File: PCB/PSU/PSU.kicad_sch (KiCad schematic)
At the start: 258 parts, among them J1 Backllight_Connector, J2 PSU_Jack, J3 PSU_Connector_Receptor, Q1 R4C, Q10 103 5G, Q11 6LS, Q12 Q, Q13 8LR, Q14 6LS, Q15 8LR, Q16 M2P, Q17 M2P, Q18 Q, Q19 M2P, Q2 K, Q20 W6, Q21 8C, Q22 8C, Q23 8C, Q24 6LS, Q25 8LB, Q26 G16, Q27 8C, Q28 W6, Q29 H15, Q3 6LS, Q30 8C, Q31 W6, Q32 K, Q33 8LR, Q34 6LS, Q35 8C, Q36 3P4J, Q37 8LR, Q4 8LR, Q5 8C, Q6 6LS, Q7 6LS, Q8 303 5H, Q9 KD 3.E, SW1 PSU-SW1, U1 D9D, U10 9742, U11 7W14, U12 J421, U13 J421, U2 TA, U3 6.5 5F, U4 MAX786CAI, U5 K2337, U6 7064, U7 5W01, U8 2556, U9 2556

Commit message: cleanup psu schematics
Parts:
- removed C1, C16, C24, C28, C36, C46, C47, C5, C59, C7: 150nF, Capacitor_SMD:C_0603_1608Metric, symbol PCM_Elektuur:C
- removed C10: 3.6nF, Capacitor_SMD:C_0603_1608Metric, symbol PCM_Elektuur:C
- removed C11, C15, C37, C44, C49: 180nF, Capacitor_SMD:C_0603_1608Metric, symbol PCM_Elektuur:C
- removed C12: 1.2uF, Capacitor_SMD:C_1206_3216Metric, symbol PCM_Elektuur:C
- removed C13, C14: 1.5uF, Capacitor_SMD:C_1206_3216Metric, symbol PCM_Elektuur:C
- removed C17, C22, C26, C29, C30, C32, C39, C40, C48, C9: 10nF, Capacitor_SMD:C_0603_1608Metric, symbol PCM_Elektuur:C
- removed C18, C42, C51, C53, C64: 120nF, Capacitor_SMD:C_0603_1608Metric, symbol PCM_Elektuur:C
- removed C19: 18nF, Capacitor_SMD:C_0603_1608Metric, symbol PCM_Elektuur:C
- removed C2: 4.7nF, Capacitor_SMD:C_0603_1608Metric, symbol PCM_Elektuur:C
- removed C20, C6: 100pF, Capacitor_SMD:C_0603_1608Metric, symbol PCM_Elektuur:C
- removed C21: 12nF, Capacitor_SMD:C_0603_1608Metric, symbol PCM_Elektuur:C
- removed C23, C34, C38, C41, C55, C58: 1.5uF, Capacitor_SMD:C_0805_2012Metric, symbol PCM_Elektuur:C
- removed C25, C27, C31, C35, C66: 1.2nF, Capacitor_SMD:C_0603_1608Metric, symbol PCM_Elektuur:C
- removed C3: 5.2uF, Capacitor_SMD:C_1206_3216Metric, symbol PCM_Elektuur:C
- removed C33, C8: 24nF, Capacitor_SMD:C_0603_1608Metric, symbol PCM_Elektuur:C
- removed C4: 2.5nF, Capacitor_SMD:C_0603_1608Metric, symbol PCM_Elektuur:C
- removed C43: 10pF, Capacitor_SMD:C_0603_1608Metric, symbol PCM_Elektuur:C
- removed C45: 33uF 20V, Capacitor_THT:C_Disc_D3.0mm_W1.6mm_P2.50mm, symbol PCM_Elektuur:C
- removed C50: 56uF 25V EC, Capacitor_THT:EC, symbol PCM_Elektuur:C
- removed C52, C60: 1nF, Capacitor_SMD:C_0603_1608Metric, symbol PCM_Elektuur:C
- removed C54, C61: 47uF 6.3v, Capacitor_THT:C_Radial_D6.3mm_H11.0mm_P2.50mm, symbol PCM_Elektuur:C
- removed C56: 47uF 6.3V, Capacitor_THT:C_Radial_D6.3mm_H11.0mm_P2.50mm, symbol PCM_Elektuur:C
- removed C57: 15uF 16V, Capacitor_THT:C_Radial_D6.3mm_H11.0mm_P2.50mm, symbol PCM_Elektuur:C
- removed C62, C65: 100nF, Capacitor_SMD:C_0603_1608Metric, symbol PCM_Elektuur:C
- removed C63: 5.1nF, Capacitor_SMD:C_0603_1608Metric, symbol PCM_Elektuur:C
- removed C67: 18uF 50V, Capacitor_THT:C_Radial_D6.3mm_H11.0mm_P2.50mm, symbol PCM_Elektuur:C
- removed D1: 8-2, Diode_SMD:D_0603_1608Metric, symbol Device:D_Zener
- removed D2: 5-9, Diode_SMD:D_0603_1608Metric, symbol PCM_Elektuur:D
- removed D3: DNP, Diode_SMD:D_1206_3216Metric, symbol PCM_Elektuur:C
- removed D4: 18, Diode_SMD:D_0603_1608Metric, symbol Device:D
- removed D5: 3^9, Diode_SMD:D_0603_1608Metric, symbol Device:D
- removed D6: DNP, Diode_SMD:D_1206_3216Metric, symbol PCM_Elektuur:R
- removed D7, D8: s.3 4F, Diode_SMD:D_1206_3216Metric, symbol PCM_Elektuur:D
- removed F1, F5: 2.5A, Fuse:Fuse_2010_5025Metric, symbol Device:Fuse
- removed F2: 830mA, Fuse:Fuse_2010_5025Metric, symbol Device:Fuse
- removed F3: 15, Fuse:Fuse_1206_3216Metric, symbol Device:Fuse
- removed F4: 10, Fuse:Fuse_1210_3225Metric, symbol Device:Fuse
- removed J1: Backllight_Connector, Connector_JST:Backllight_Connector, symbol Connector_Generic:Conn_01x04
- removed J2: PSU_Jack, PSU:PSU_Jack, symbol Connector:Jack-DC
- removed J3: PSU_Connector_Receptor, PSU:PSU_Connector_Receptor, symbol Connector_Generic:Conn_02x20_Top_Bottom
- removed JX1: Main Battery, symbol Connector:Conn_01x02_Pin
- removed L1: 10uH, Inductor_THT:L_Radial_D7.5mm_P5.00mm_Fastron_07P, symbol PCM_Elektuur:L
- removed L2, L5: 10uH, Inductor_THT:L_Radial_D10.0mm_P5.00mm_Fastron_07M, symbol PCM_Elektuur:L
- removed L3: 68uH, Inductor_SMD:L_Coilcraft_LPS5030, symbol PCM_Elektuur:L
- removed L4: 470uH, Inductor_SMD:L_Coilcraft_LPS5030, symbol PCM_Elektuur:L
- removed Q1: R4C, PC110:3D, symbol Device:D_Zener_Dual_CommonCathode_AAK_Split
- removed Q10: 103 5G, Package_TO_SOT_SMD:SOT-powerT, symbol PSU:103_5G
- removed Q11, Q14: 6LS, Package_TO_SOT_SMD:SOT-416, symbol PCM_Transistor_BJT_AKL:Q_PNP_Generic_BEC
- removed Q12: Q, PC110:3D, symbol Device:D_Zener_Dual_CommonAnode_KAK
- removed Q13, Q15, Q33, Q37: 8LR, Package_TO_SOT_SMD:SOT-416, symbol PCM_Transistor_BJT_AKL:Q_NPN_Generic_BEC
- removed Q16, Q17, Q19: M2P, PC110:3D, symbol Device:D_Zener_Dual_CommonAnode_KAK
- removed Q18: Q, PC110:3D, symbol Device:D_Dual_CommonCathode_AKA
- removed Q2: K, PC110:3D, symbol Device:D_Dual_Series_KAC_Parallel
- removed Q20, Q28, Q31: W6, PC110:3D, symbol Device:D_Dual_CommonCathode_AKA
- removed Q21: 8C, Package_TO_SOT_SMD:SOT-416, symbol Simulation_SPICE:NPN
- removed Q22, Q5: 8C, Package_TO_SOT_SMD:SOT-416, symbol PCM_Transistor_BJT_AKL:Q_NPN_Generic_CEB
- removed Q23, Q27, Q30, Q35: 8C, Package_TO_SOT_SMD:SOT-416, symbol PCM_Transistor_BJT_AKL:Q_NPN_Generic_BEC
- removed Q24: 6LS, Package_TO_SOT_SMD:SOT-416, symbol PCM_Transistor_BJT_AKL:Q_PNP_Generic_CEB
- removed Q25: 8LB, Package_TO_SOT_SMD:SOT-416, symbol PCM_Transistor_BJT_AKL:Q_NPN_Generic_BEC
- removed Q26: G16, Package_TO_SOT_SMD:SOT-23-PC110, symbol PCM_Transistor_MOSFET_AKL:2N7002AQ
- removed Q29: H15, Package_TO_SOT_SMD:SOT-23-PC110, symbol Transistor_FET:AO3401A
- removed Q3, Q34, Q6, Q7: 6LS, Package_TO_SOT_SMD:SOT-416, symbol Simulation_SPICE:PNP
- removed Q32: K, PC110:3D, symbol Device:D_Dual_Series_ACK_Parallel
- removed Q36: 3P4J, Package_TO_SOT_SMD:TO-252-2, symbol PCM_Elektuur:Th
- removed Q4: 8LR, Package_TO_SOT_SMD:SOT-416, symbol PCM_Transistor_BJT_AKL:Q_NPN_Generic_CEB
- removed Q8: 303 5H, Package_TO_SOT_SMD:SOT-powerT, symbol PSU:103_5G
- removed Q9: KD 3.E, Package_TO_SOT_SMD:SOT-89-3, symbol Regulator_Linear:L78L05_SOT89
- removed R1, R108, R50, R82: DNP, Resistor_SMD:R_0603_1608Metric, symbol PCM_Elektuur:R
- removed R10, R2, R21, R31, R70, R74, R83, R87, R90: 470k, Resistor_SMD:R_0603_1608Metric, symbol PCM_Elektuur:R
- removed R100, R110: 7.5k, Resistor_SMD:R_0603_1608Metric, symbol PCM_Elektuur:R
- removed R101, R109, R45, R62, R69, R81: 200k, Resistor_SMD:R_0603_1608Metric, symbol PCM_Elektuur:R
- removed R102, R49, R53, R78: 300k, Resistor_SMD:R_0603_1608Metric, symbol PCM_Elektuur:R
- removed R103, R11, R114, R117, R13, R17, R19, R20, R30, R33, R35, R4, R44, R52, R61, R63, R64, R85, R86: 10k, Resistor_SMD:R_0603_1608Metric, symbol PCM_Elektuur:R
- removed R104, R118, R48: 100, Resistor_SMD:R_0603_1608Metric, symbol PCM_Elektuur:R
- removed R105, R15, R22, R5, R54, R57, R59, R77, R80, R84, R92: 100k, Resistor_SMD:R_0603_1608Metric, symbol PCM_Elektuur:R
- removed R106, R27, R39, R41, R51, R58, R60: 4.7k, Resistor_SMD:R_0603_1608Metric, symbol PCM_Elektuur:R
- removed R107: 2k, Resistor_SMD:R_0603_1608Metric, symbol PCM_Elektuur:R
- removed R111: 33, Resistor_SMD:R_0603_1608Metric, symbol PCM_Elektuur:R
- removed R112, R113, R18, R9: 20k, Resistor_SMD:R_0603_1608Metric, symbol PCM_Elektuur:R
- removed R115: 11K, Resistor_SMD:R_0603_1608Metric, symbol PCM_Elektuur:R
- removed R116: 15k, Resistor_SMD:R_0603_1608Metric, symbol PCM_Elektuur:R
- removed R12: 2.2k, Resistor_SMD:R_0603_1608Metric, symbol PCM_Elektuur:R
- removed R14: 12k, Resistor_SMD:R_0603_1608Metric, symbol PCM_Elektuur:R
- removed R16: 130k, Resistor_SMD:R_0603_1608Metric, symbol PCM_Elektuur:R
- removed R23, R25, R32, R34: 0.1, Resistor_SMD:R_1206_3216Metric, symbol PCM_Elektuur:R
- removed R24: 220, Resistor_SMD:R_0603_1608Metric, symbol PCM_Elektuur:R
- removed R26: 103 (RT1), Resistor_SMD:R_1206_3216Metric, symbol PCM_Elektuur:R
- removed R28: 0, Resistor_SMD:R_0603_1608Metric, symbol PCM_Elektuur:R
- removed R29: 103 (RT2), Resistor_SMD:R_1206_3216Metric, symbol PCM_Elektuur:R
- removed R3, R36, R65, R71, R72, R75, R76, R93: 1k, Resistor_SMD:R_0603_1608Metric, symbol PCM_Elektuur:R
- removed R37: 120, Resistor_SMD:R_0603_1608Metric, symbol PCM_Elektuur:R
- removed R38, R6: 470, Resistor_SMD:R_0603_1608Metric, symbol PCM_Elektuur:R
- removed R40: 0.22, Resistor_SMD:R_1206_3216Metric, symbol PCM_Elektuur:R
- removed R42, R47, R67, R68, R73, R79, R94: 47k, Resistor_SMD:R_0603_1608Metric, symbol PCM_Elektuur:R
- removed R43, R56: 300, Resistor_SMD:R_0603_1608Metric, symbol PCM_Elektuur:R
- removed R46, R55, R88, R89: 1M, Resistor_SMD:R_0603_1608Metric, symbol PCM_Elektuur:R
- removed R66: DNP, Resistor_SMD:R_0603_1608Metric, symbol PCM_Elektuur:C
- removed R7, R8: 0.1, Resistor_SMD:R_1210_3225Metric, symbol PCM_Elektuur:R
- removed R91: DNP, Resistor_SMD:R_1206_3216Metric, symbol PCM_Elektuur:R
- removed R95, R97: DNP, Resistor_SMD:R_1206_3216Metric, symbol PCM_Elektuur:C
- removed R96: 1.8k, Resistor_SMD:R_0603_1608Metric, symbol PCM_Elektuur:R
- removed R98, R99: 0, Resistor_SMD:R_1206_3216Metric, symbol PCM_Elektuur:R
- removed SW1: PSU-SW1, PSU:PSU-SW1, symbol Switch:SW_Push
- removed U1: D9D, Package_TO_SOT_SMD:SOT-23-5, symbol Power_Management:BD48ExxG
- removed U10: 9742, Package_SO:SSOP-16_4.4x5.2mm_P0.65mm, symbol PSU:9742
- removed U11: 7W14, PSU:SSOP-8-PSU, symbol 74xGxx:74LVC3G14
- removed U12, U13: J421, Package_SO:SOP-8_3.9x4.9mm_P1.27mm, symbol Transistor_FET:FDS2734
- removed U2: TA, Package_TO_SOT_SMD:SOT-23-5, symbol PSU:TA
- removed U3: 6.5 5F, Package_TO_SOT_SMD:SOT-23-6_Handsoldering, symbol PSU:6.5_5F
- removed U4: MAX786CAI, Package_SO:TSSOP-28_6.1x9.7mm_P0.65mm, symbol PSU:MAX786CAI
- removed U5: K2337, Package_SO:SOP-8_3.9x4.9mm_P1.27mm, symbol Transistor_FET:Si4542DY
- removed U6: 7064, Package_SO:TSSOP-14_4.4x5mm_P0.65mm, symbol Device:Opamp_Quad
- removed U7: 5W01, PSU:SSOP-8-PSU, symbol Device:Opamp_Dual
- removed U8, U9: 2556, Package_SO:SOP-8_3.9x4.9mm_P1.27mm, symbol Transistor_FET:FDS2734
- added C65: 0.1u, symbol PSU:C
- added CN3: 179029-1, symbol PSU:CN_40
- added CN4: DF13- 4P-1.25V, symbol PSU:CN_4+PAD
- added D10: MA741WA, symbol PSU:D_ANODE-COM
- added D11: MAZ8039-H, symbol PSU:Z
- added F6: 630mA, symbol PSU:F
- added R107: 1k, symbol PSU:R
- added R108: 47k, symbol PSU:R
- added R109, R110: 4.7k, symbol PSU:R
- added R111: (no value), symbol PSU:R
- added RT1, RT2: 103HT-xx, symbol PSU:RL
- added SW1: (no value), symbol PSU:SW_PAD
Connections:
- net GND: now also C65.1, CN3.24, CN3.25, CN3.29, CN3.32, CN3.37, CN3.5, CN3.7, CN3.9, CN4.3, R108.2, R109.1, R110.1
- new net: D10.1 (C1), R110.2, RT2.2
- new net: D10.2 (A), D11.1 (C), R111.1
- new net: D10.3 (C2), R109.2, RT1.1
- new net: C65.2, CN4.4, F6.1
- new net: R107.1, R108.1, SW1.2
- new net +12V: CN3.12
- new net +12V_ENABLE: CN3.34
- new net +3V3: CN3.28, CN3.8
- new net +5V_STBY: CN3.16, SW1.1
- new net +5V_SW: CN3.10, CN3.11, CN3.31, RT1.2, RT2.1
- new net BAT_MONT_VOLT: CN3.21
- new net BAT_MON_CHGCURR: CN3.2
- new net BAT_MON_DISCHGCURR: CN3.1
- new net CHG_CONT_1: CN3.19
- new net CHG_CONT_2: CN3.39
- new net CHG_MONPWR_EN: CN3.18
- new net CHG_SUBPWR: CN3.6
- new net EXT_DEV_DETSW: CN3.33, R107.2
- new net LCD_BKLIT_ADJ: CN3.20, CN4.2
- new net LCD_BKLIT_INVEN: CN3.40, CN4.1
- new net MONT_VOLT_ENABLE: CN3.38
- new net TEMPSENS: CN3.22, D11.2 (A), R111.2
- new net VAA_LCD: CN3.13
- new net VAA_LCD_ADJ: CN3.15
- new net VAA_LCD_ENABLE: CN3.35
- new net VIN_AC_DETECT: CN3.26
- new net VIN_AC_MON_VOLT: CN3.27
- new net VREF: CN3.30
- new net VSW: CN3.14, F6.2
- new net VSW_ENABLE_1: CN3.17
- new net VSW_ENABLE_2: CN3.36
- new net VSYS: CN3.23, CN3.3, CN3.4
- no-connect marks 3 -> 2
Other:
- added sheet AC Input (acinput.kicad_sch)
- added sheet Battery Charge, Monitor (batchgmon.kicad_sch)
- added sheet DC-DC (dcdc.kicad_sch)
- added sheet Standby Power (stdbypwr.kicad_sch)
- note added: "+12V"
- note added: "+3.3"
- note added: "+5V"
- note added: "+5V_STBY"
- note added: "LCD_VAA"
- note added: "SOC SSFC? Quick-Acting"
- note added: "VSW"
- note added: "VSYS"
- company: Recreated by: Ahmad Byagowi -> (none)
- title: PC110 Power Supply Unit -> IBM 39H4552 : PalmTop PC110 Power supply module

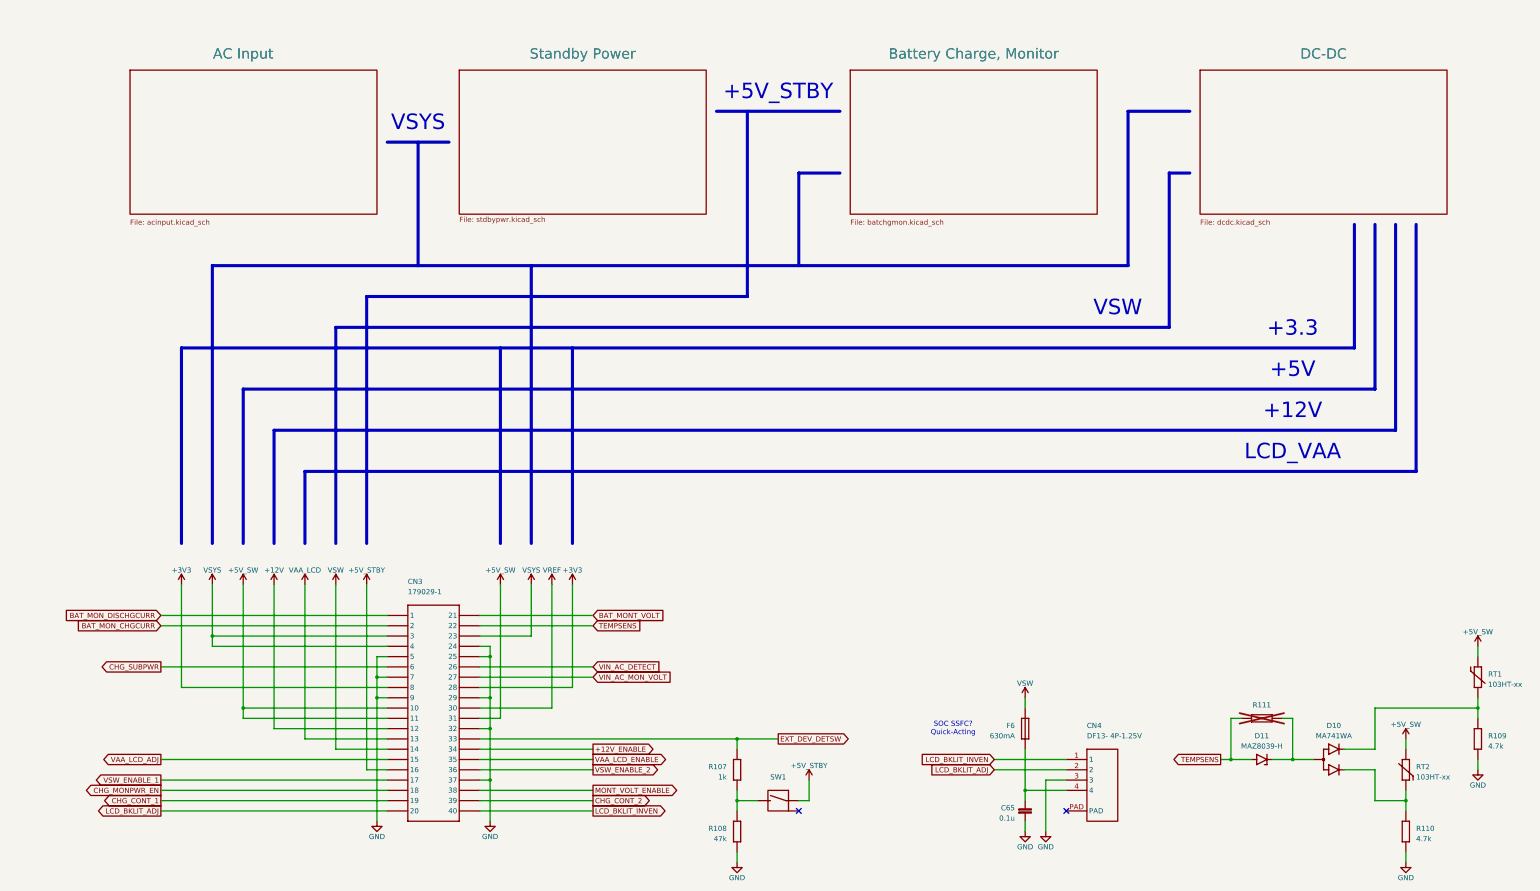
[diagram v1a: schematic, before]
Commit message: edit layout and misspelled word(not changed sch)
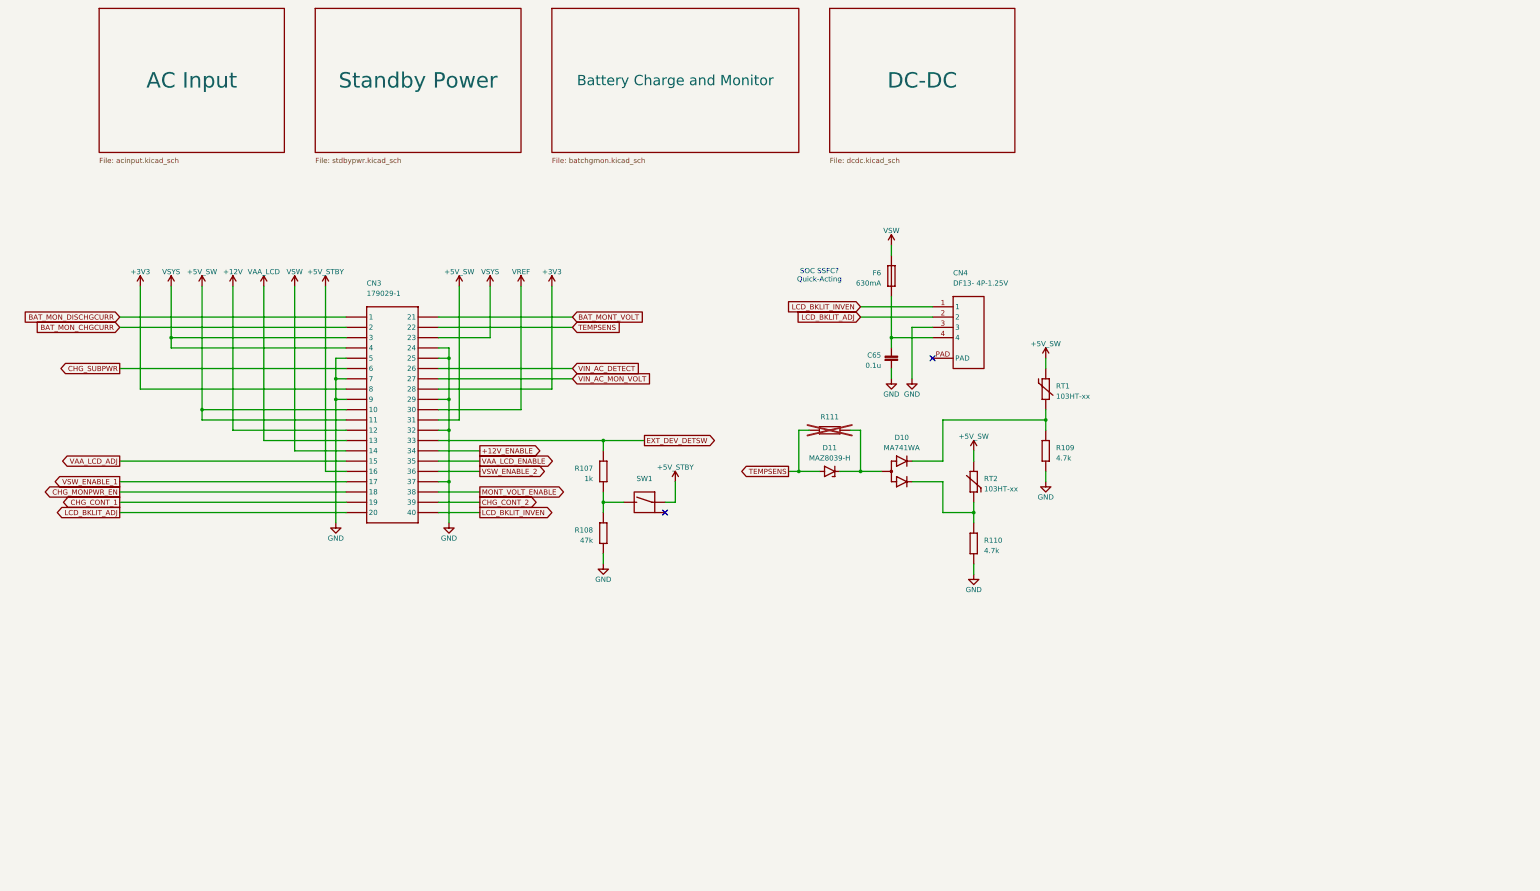
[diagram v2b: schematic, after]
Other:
- sheet Battery Charge, Monitor renamed Battery Charge and Monitor
- note removed: "+12V"
- note removed: "+3.3"
- note removed: "+5V"
- note removed: "+5V_STBY"
- note removed: "LCD_VAA"
- note removed: "VSW"
- note removed: "VSYS"
- moved on the sheet: C65, CN3, CN4, D10, D11, F6, R107, R108, R109, R110, R111, RT1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
